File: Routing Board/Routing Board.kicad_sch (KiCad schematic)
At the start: 44 parts, among them J1 ETC SIG, J10 PCU CAN, J11 PCU PWR, J2 ETC PWR, J3 ETC CAN, J4 SCU CAN, J5 SCU SIG, J6 BSPD PWR, J7 BSPD SIG, J8 SCU PWR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

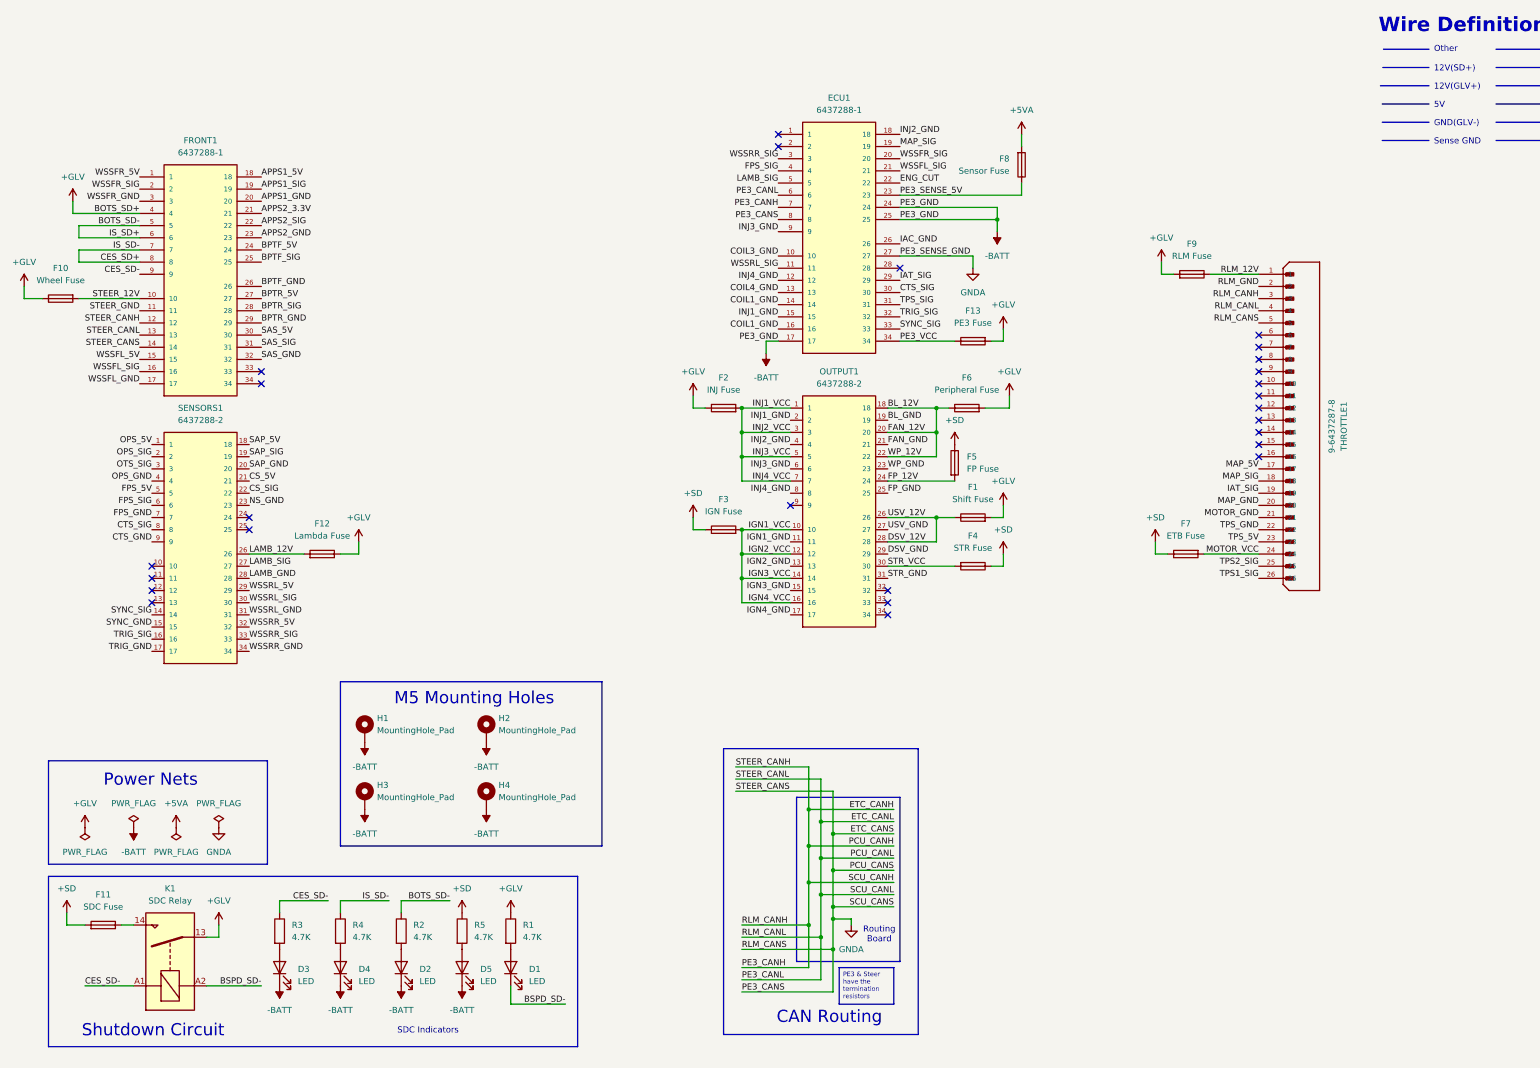
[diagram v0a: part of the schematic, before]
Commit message: feat: begin SCU, RLM, PCU, ETC. update SWU
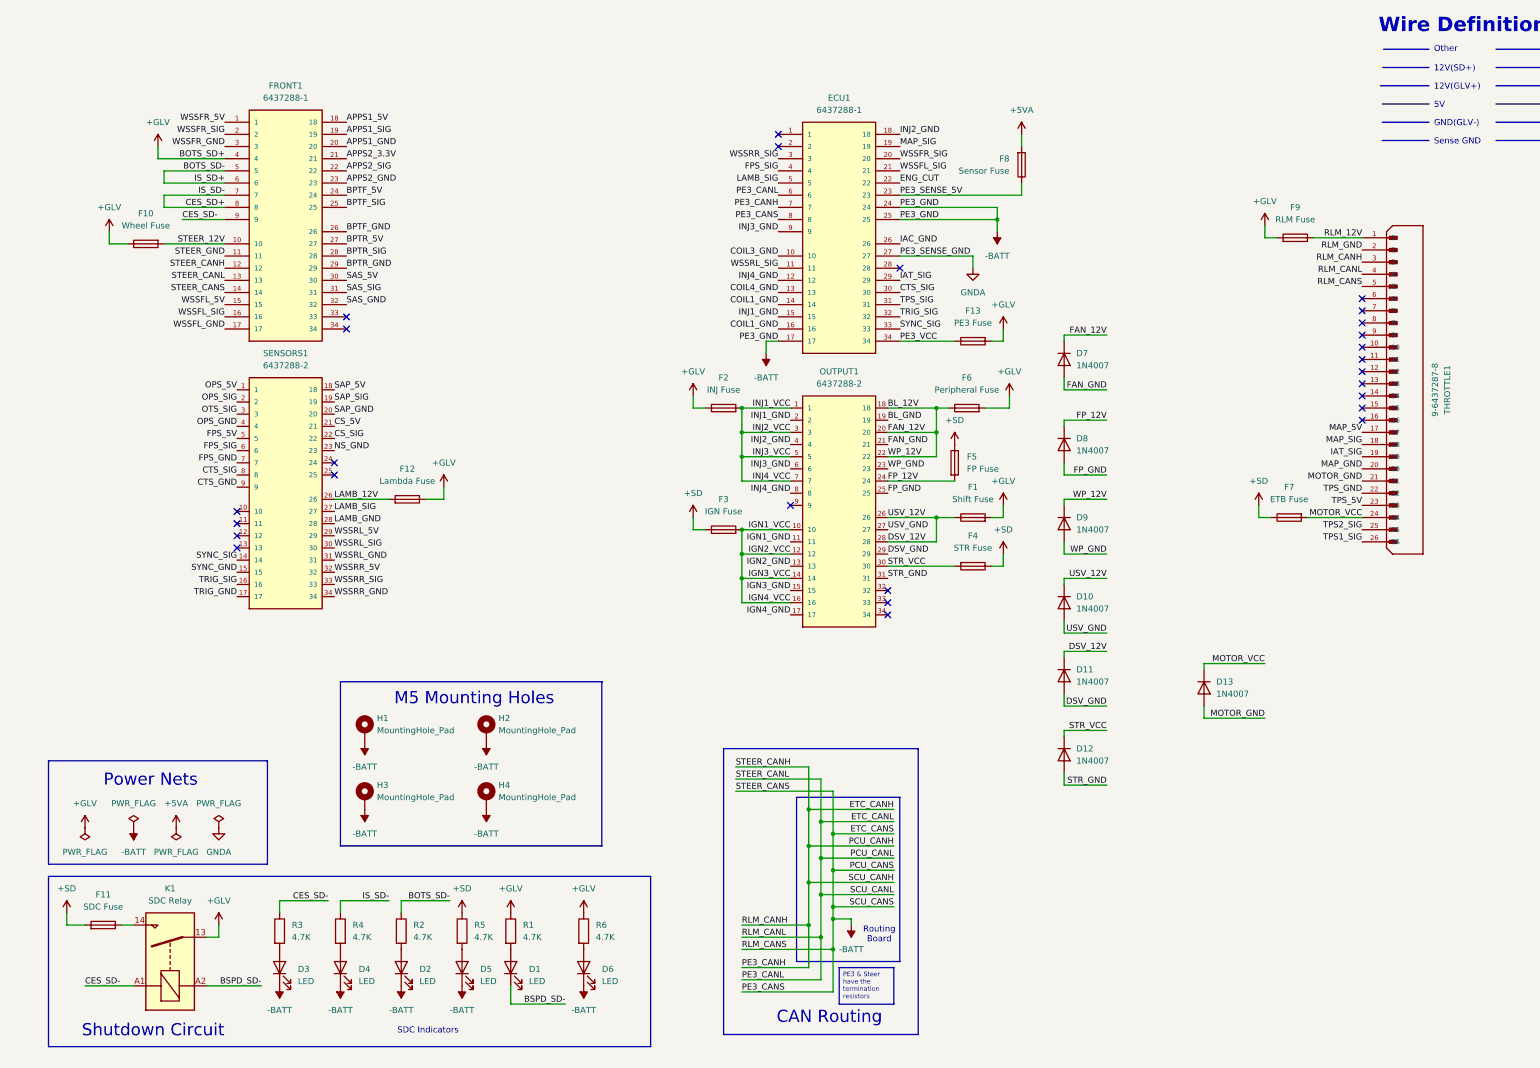
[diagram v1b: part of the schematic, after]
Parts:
- added D10, D11, D12, D13, D7, D8, D9: 1N4007, Diode_THT:D_DO-41_SOD81_P10.16mm_Horizontal, symbol Diode:1N4007
- added D6: LED, LED_SMD:LED_0603_1608Metric, symbol Device:LED
- added R6: 4.7K, symbol Device:R
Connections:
- net +GLV: now also R6.1
- net -BATT: now also ECU1.8, FRONT1.14, J10.3 (Pin_3), J3.3 (Pin_3), J4.3 (Pin_3), THROTTLE1.5, D6.1 (K)
- net BL_12V: now also D7.1 (K), D9.1 (K)
- net DSV_12V: now also D10.1 (K), D11.1 (K)
- net DSV_GND: now also D11.2 (A)
- net FAN_GND: now also D7.2 (A)
- net FP_12V: now also D8.1 (K)
- net FP_GND: now also D8.2 (A)
- net GNDA: no longer ECU1.8, FRONT1.14, J10.3 (Pin_3), J3.3 (Pin_3), J4.3 (Pin_3), THROTTLE1.5
- net MOTOR_GND: now also D13.2 (A)
- net MOTOR_VCC: now also D13.1 (K)
- net STR_GND: now also D12.2 (A)
- net STR_VCC: now also D12.1 (K)
- net USV_GND: now also D10.2 (A)
- net WP_GND: now also D9.2 (A)
- new net: D6.2 (A), R6.2
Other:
- moved on the sheet: F10, F12, F7, F9, FRONT1, SENSORS1, THROTTLE1
